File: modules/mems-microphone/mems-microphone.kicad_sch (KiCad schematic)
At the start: 6 parts

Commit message: begin work on pcb layout for MEMS module
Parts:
- M1: footprint MegaCastle:MegaCastle2x5-Module -> MegaCastle:MegaCastle2x5-Module-M9C4
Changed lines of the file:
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@@
 			)
 		)
-		(property "Footprint" "MegaCastle:MegaCastle2x5-Module"
+		(property "Footprint" "MegaCastle:MegaCastle2x5-Module-M9C4"
 			(at 91.44 99.06 0)
 			(effects

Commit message: add footprints for passives for MEMS mic module
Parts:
- C1: footprint (none) -> Capacitor_SMD:C_1206_3216Metric
- R1, R2, R3: footprint (none) -> Resistor_SMD:R_0603_1608Metric
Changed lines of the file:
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@@
 			)
 		)
-		(property "Footprint" ""
+		(property "Footprint" "Capacitor_SMD:C_1206_3216Metric"
 			(at 51.7652 59.69 0)
 			(effects
@@
 			)
 		)
-		(property "Footprint" ""
+		(property "Footprint" "Resistor_SMD:R_0603_1608Metric"
 			(at 91.44 62.738 90)
 			(effects
@@
 			)
 		)
-		(property "Footprint" ""
+		(property "Footprint" "Resistor_SMD:R_0603_1608Metric"
 			(at 89.408 49.53 90)
 			(effects
@@
 			)
 		)
-		(property "Footprint" ""
+		(property "Footprint" "Resistor_SMD:R_0603_1608Metric"
 			(at 91.44 69.342 90)
 			(effects

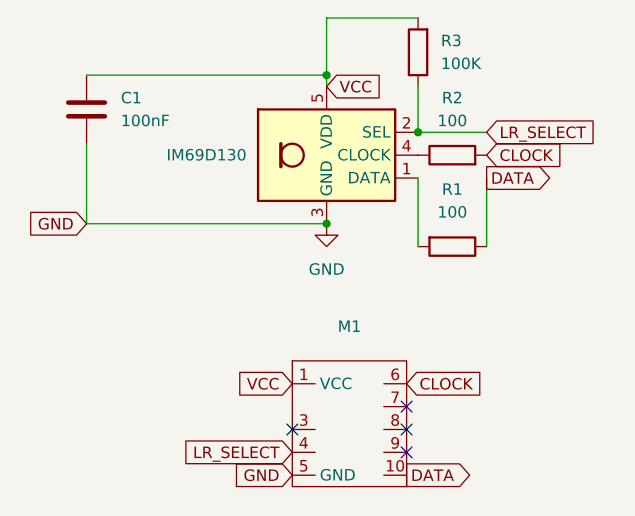
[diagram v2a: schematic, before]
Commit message: update footprint for mems microphone
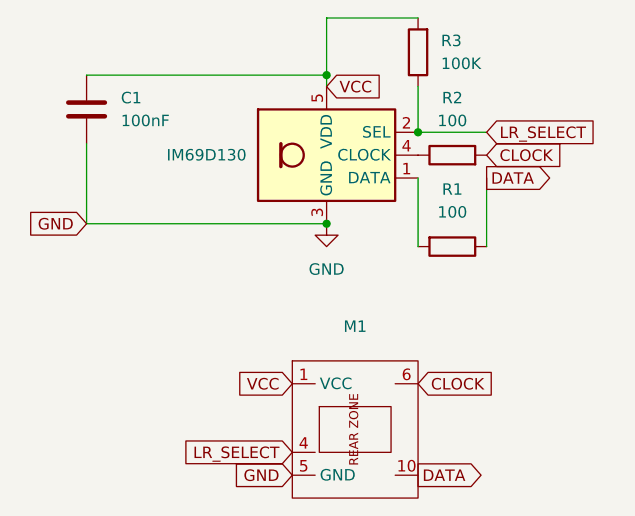
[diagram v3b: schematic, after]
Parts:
- removed M1: ~, MegaCastle:MegaCastle2x5-Module-M9C4, symbol MegaCastle:MegaCastle2x5-Module
- added M1: ~, MegaCastle:MegaCastle2x5-Module-I6.4x7.9-M9C4, symbol MegaCastle:MegaCastle2x5-Module-I6.4x7.9-M9C4
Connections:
- net CLOCK: now also M1.6
- net DATA: now also M1.10
- net GND: now also M1.5 (GND)
- net LR_SELECT: now also M1.4
- net VCC: now also M1.1 (VCC)
- no-connect marks 4 -> 0
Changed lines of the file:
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@@
 		(color 0 0 0 0)
-	)
-	(no_connect
-		(at 86.36 88.9)
-	)
-	(no_connect
-		(at 73.66 91.44)
-	)
-	(no_connect
-		(at 86.36 93.98)
-	)
-	(no_connect
-		(at 86.36 91.44)
 	)
 	(wire
@@
 	(global_label "DATA"
 		(shape output)
-		(at 86.36 96.52 0)
+		(at 87.63 96.52 0)
 		(fields_autoplaced yes)
 		(effects
@@
 		)
 		(property "Intersheetrefs" "${INTERSHEET_REFS}"
-			(at 93.76 96.52 0)
+			(at 95.03 96.52 0)
 			(effects
 				(font
@@
 	(global_label "CLOCK"
 		(shape input)
-		(at 86.36 86.36 0)
+		(at 87.63 86.36 0)
 		(fields_autoplaced yes)
 		(effects
@@
 		)
 		(property "Intersheetrefs" "${INTERSHEET_REFS}"
-			(at 95.5138 86.36 0)
+			(at 96.7838 86.36 0)
 			(effects
 				(font
@@
 				(justify left)
 				(hide yes)
+			)
+		)
+	)
+	(symbol
+		(lib_id "MegaCastle:MegaCastle2x5-Module-I6.4x7.9-M9C4")
+		(at 80.01 91.44 0)
+		(unit 1)
+		(exclude_from_sim no)
+		(in_bom yes)
+		(on_board yes)
+		(dnp no)
+		(fields_autoplaced yes)
+		(property "Reference" "M1"
+			(at 80.645 80.01 0)
+			(effects
+				(font
+					(size 1.27 1.27)
+				)
+			)
+		)
+		(property "Value" "~"
+			(at 80.645 82.55 0)
+			(effects
+				(font
+					(size 1.27 1.27)
+				)
+			)
+		)
+		(property "Footprint" "MegaCastle:MegaCastle2x5-Module-I6.4x7.9-M9C4"
+			(at 80.01 104.14 0)
+			(effects
+				(font
+					(size 1.27 1.27)
+				)
+				(hide yes)
+			)
+		)
+		(property "Datasheet" ""
+			(at 80.01 86.36 0)
+			(effects
+				(font
+					(size 1.27 1.27)
+				)
+				(hide yes)
+			)
+		)
+		(property "Description" "Generated using footprint-gen .. 6.4 6 5 M9C4"
+			(at 80.01 91.44 0)
+			(effects
+				(font
+					(size 1.27 1.27)
+				)
+				(hide yes)
+			)
+		)
+		(pin "4"
+		)
+		(pin "1"
+		)
+		(pin "5"
+		)
+		(pin "10"
+		)
+		(pin "6"
+		)
+		(instances
+			(project ""
+				(path "/e00fa767-96d8-4813-9886-8a9eb239d9ae"
+					(reference "M1")
+					(unit 1)
+				)
 			)
 		)
@@
 					(unit 1)
 				)
-			)
-		)
-	)
-	(symbol
-		(lib_id "MegaCastle:MegaCastle2x5-Module")
-		(at 80.01 90.17 0)
-		(unit 1)
-		(exclude_from_sim no)
-		(in_bom yes)
-		(on_board yes)
-		(dnp no)
-		(fields_autoplaced yes)
-		(property "Reference" "M1"
-			(at 80.01 80.01 0)
-			(effects
-				(font
-					(size 1.27 1.27)
-				)
-			)
-		)
-		(property "Value" "~"
-			(at 80.01 82.55 0)
-			(effects
-				(font
-					(size 1.27 1.27)
-				)
-			)
-		)
-		(property "Footprint" "MegaCastle:MegaCastle2x5-Module-M9C4"
-			(at 91.44 99.06 0)
-			(effects
-				(font
-					(size 1.27 1.27)
-				)
-				(hide yes)
-			)
-		)
-		(property "Datasheet" ""
-			(at 97.79 90.17 0)
-			(effects
-				(font
-					(size 1.27 1.27)
-				)
-				(hide yes)
-			)
-		)
-		(property "Description" ""
-			(at 80.01 90.17 0)
-			(effects
-				(font
-					(size 1.27 1.27)
-				)
-				(hide yes)
-			)
-		)
-		(pin "8"
-		)
-		(pin "6"
-		)
-		(pin "5"
-		)
-		(pin "4"
-		)
-		(pin "7"
-		)
-		(pin "10"
-		)
-		(pin "9"
-		)
-		(pin "3"
-		)
-		(pin "1"
-		)
-		(instances
-			(project ""
-				(path "/e00fa767-96d8-4813-9886-8a9eb239d9ae"
-					(reference "M1")
-					(unit 1)
-				)
